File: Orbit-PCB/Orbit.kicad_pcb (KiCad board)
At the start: 2 copper layers, 303.2 x 145.3 mm, 296 parts, among them J1 PJ-3200B-4A, J10 Breakaway_Tabs, J11 PJ-3200B-4A, J12 AVR-ISP-6, J13 Breakaway_Tabs, J14 Breakaway_Tabs, J17 Breakaway_Tabs, J18 Breakaway_Tabs, J19 Breakaway_Tabs, J2 AVR-ISP-6, J20 Breakaway_Tabs, J3 Breakaway_Tabs, J5 Breakaway_Tabs, J6 Breakaway_Tabs, J7 Breakaway_Tabs, J9 Breakaway_Tabs, Q1 2N7002, Q2 2N7002, SW1 SW_Push, SW2 SW_Push, U1 ATmega32U4-MU, U2 PRTR5V0U2X, U3 ATmega32U4-MU, U4 PRTR5V0U2X, Y1 16MHz, Y2 16MHz

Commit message: Remove zones
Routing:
- net GND: track 1321.2 -> 0.00 mm, vias 32 -> 0
- net GNDA: track 1114.9 -> 0.00 mm, vias 39 -> 0
- net +5V: track 1023.8 -> 0.00 mm, vias 10 -> 0
- net +5VA: track 979.0 -> 0.00 mm, vias 8 -> 0
- net LEDGND: track 700.6 -> 0.00 mm, vias 12 -> 0
- net LEDGND-R: track 666.7 -> 0.00 mm, vias 16 -> 0
- net ROW0-R: track 242.9 -> 0.00 mm, vias 5 -> 0
- net ROW4-R: track 240.5 -> 0.00 mm, vias 8 -> 0
- net ROW0: track 195.1 -> 0.00 mm, vias 4 -> 0
- net ROW1-R: track 187.7 -> 0.00 mm, vias 2 -> 0
- net COL0: track 178.7 -> 0.00 mm
- net LEDIND-3-R: track 174.4 -> 0.00 mm, vias 4 -> 0
- net COL6: track 172.3 -> 0.00 mm, vias 2 -> 0
- net ROW1: track 171.7 -> 0.00 mm, vias 2 -> 0
- net COL1: track 171.4 -> 0.00 mm, vias 1 -> 0
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- removed copper zone on B.Cu, net GND
- removed copper zone on F.Cu, net GND
- removed copper zone on B.Cu, net GNDA
- removed copper zone on F.Cu, net GNDA

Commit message: Progress
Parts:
- removed R1, R45: 10k, Resistors_SMD:R_0805
- added FID4: Fiducial, Fiducials:Fiducial_1mm_Dia_2.54mm_Outer_CopperTop, B.Cu at (32.5, 15.9)
- added FID5: Fiducial, Fiducials:Fiducial_1mm_Dia_2.54mm_Outer_CopperTop, B.Cu at (331.0, 15.9)
- added FID6: Fiducial, Fiducials:Fiducial_1mm_Dia_2.54mm_Outer_CopperTop, B.Cu at (32.5, 156.4)
- moved J12 61.0 mm to (238.1, 92.1), turned to 180 degrees
- moved Q2 18.6 mm to (212.2, 128.3)
- moved R81 18.6 mm to (216.2, 128.3)
- moved R67 16.0 mm to (241.4, 105.3), turned to 180 degrees
- moved C11 14.5 mm to (239.4, 108.0), turned to 0 degrees
- moved D57 14.4 mm to (202.3, 100.1)
- moved R68 14.4 mm to (202.3, 105.6)
- moved D43 14.3 mm to (202.4, 61.9)
- moved D50 14.3 mm to (202.4, 81.0)
- moved D58 14.3 mm to (221.6, 97.6)
- moved R53 14.3 mm to (202.4, 67.5)
- moved R60 14.3 mm to (202.4, 86.5)
- moved R69 14.3 mm to (221.6, 103.2)
- moved R88 13.8 mm to (228.5, 106.3), turned to 0 degrees
- moved C10 12.5 mm to (237.1, 121.2), turned to 0 degrees
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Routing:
- net +5VA: track 0.00 -> 796.6 mm, vias 0 -> 10
- net LEDGND-R: track 0.00 -> 323.1 mm, vias 0 -> 6
- net GNDA: track 0.00 -> 300.5 mm, vias 0 -> 4
- net ROW0-R: track 0.00 -> 222.2 mm, vias 0 -> 4
- net ROW1-R: track 0.00 -> 192.5 mm, vias 0 -> 4
- net ROW2-R: track 0.00 -> 172.9 mm, vias 0 -> 4
- net COL5-R: track 0.00 -> 165.3 mm, vias 0 -> 1
- net ROW3-R: track 0.00 -> 156.5 mm, vias 0 -> 4
- net COL6-R: track 0.00 -> 154.9 mm
- net COL0-R: track 0.00 -> 147.7 mm, vias 0 -> 6
- net COL4-R: track 0.00 -> 133.8 mm, vias 0 -> 1
- net ROW4-R: track 0.00 -> 132.3 mm, vias 0 -> 2
- net COL3-R: track 0.00 -> 111.9 mm, vias 0 -> 1
- net LEDIND-1-R: track 0.00 -> 100.4 mm, vias 0 -> 2
- net LEDIND-3-R: track 0.00 -> 99.5 mm, vias 0 -> 2
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
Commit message: Continued progress
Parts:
- moved J2 23.6 mm to (154.4, 117.5), turned to 0 degrees
- moved D13 14.3 mm to (127.8, 59.5)
- moved D20 14.3 mm to (127.8, 78.6)
- moved D27 14.3 mm to (127.8, 97.6)
- moved R16 14.3 mm to (127.8, 65.1)
- moved R23 14.3 mm to (127.8, 84.1)
- moved D33 14.2 mm to (137.7, 118.3)
- moved C3 4.49 mm to (134.6, 112.8)
- moved R38 2.77 mm to (149.5, 125.2)
- moved C4 1.61 mm to (134.1, 118.5)
- moved R25 1.45 mm to (123.2, 103.3)
- moved R31 1.26 mm to (140.9, 102.8)
- moved C6 0.63 mm to (125.0, 105.7)
- moved R41 0.13 mm to (145.9, 43.0)
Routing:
- net LEDGND-R: track 323.1 -> 667.0 mm, vias 6 -> 21
- net GNDA: track 300.5 -> 544.8 mm, vias 4 -> 6
- net +5VA: track 796.6 -> 948.0 mm, vias 10 -> 14
- net GND: track 0.00 -> 136.8 mm
- net D+: track 0.00 -> 79.9 mm
- net D-: track 0.00 -> 79.0 mm
- net +5V: track 0.00 -> 73.5 mm
- net RESET-R: track 37.4 -> 84.6 mm, vias 2 -> 3
- net COL1-R: track 82.9 -> 117.4 mm, vias 2 -> 4
- net VCC: track 0.00 -> 24.7 mm, vias 0 -> 2
- net Net-(R44-Pad1): track 0.00 -> 18.6 mm, vias 0 -> 2
- net Net-(MX68-Pad4): track 0.00 -> 17.5 mm
- net Net-(D69-Pad2): track 0.00 -> 16.3 mm
- net COL4: track 0.00 -> 15.4 mm
- net COL3: track 0.00 -> 15.4 mm
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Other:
- net class POWER: trace_width 0.381 -> 0.254

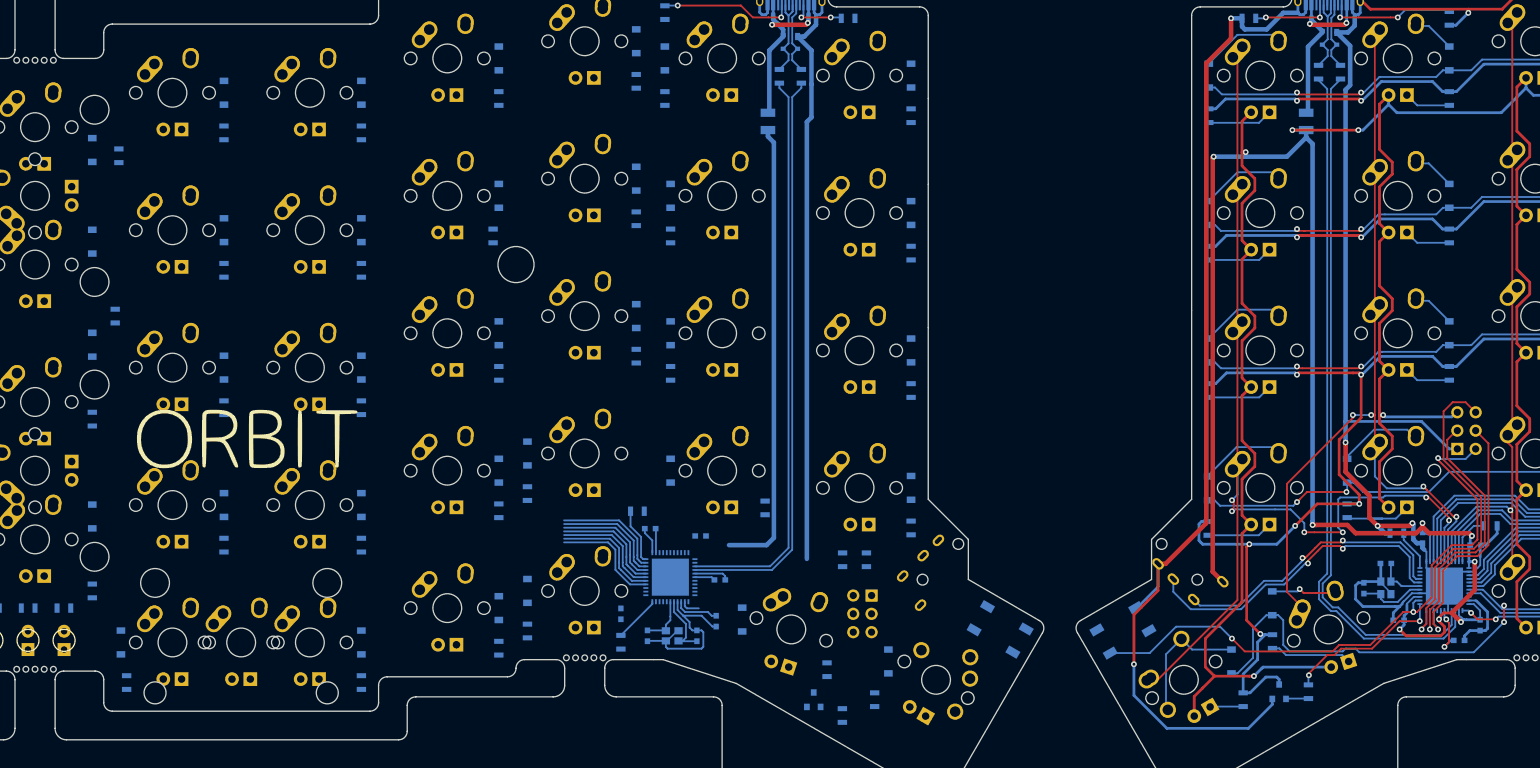
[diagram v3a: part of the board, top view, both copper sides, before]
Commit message: Add schottky divide to vcc/vbus
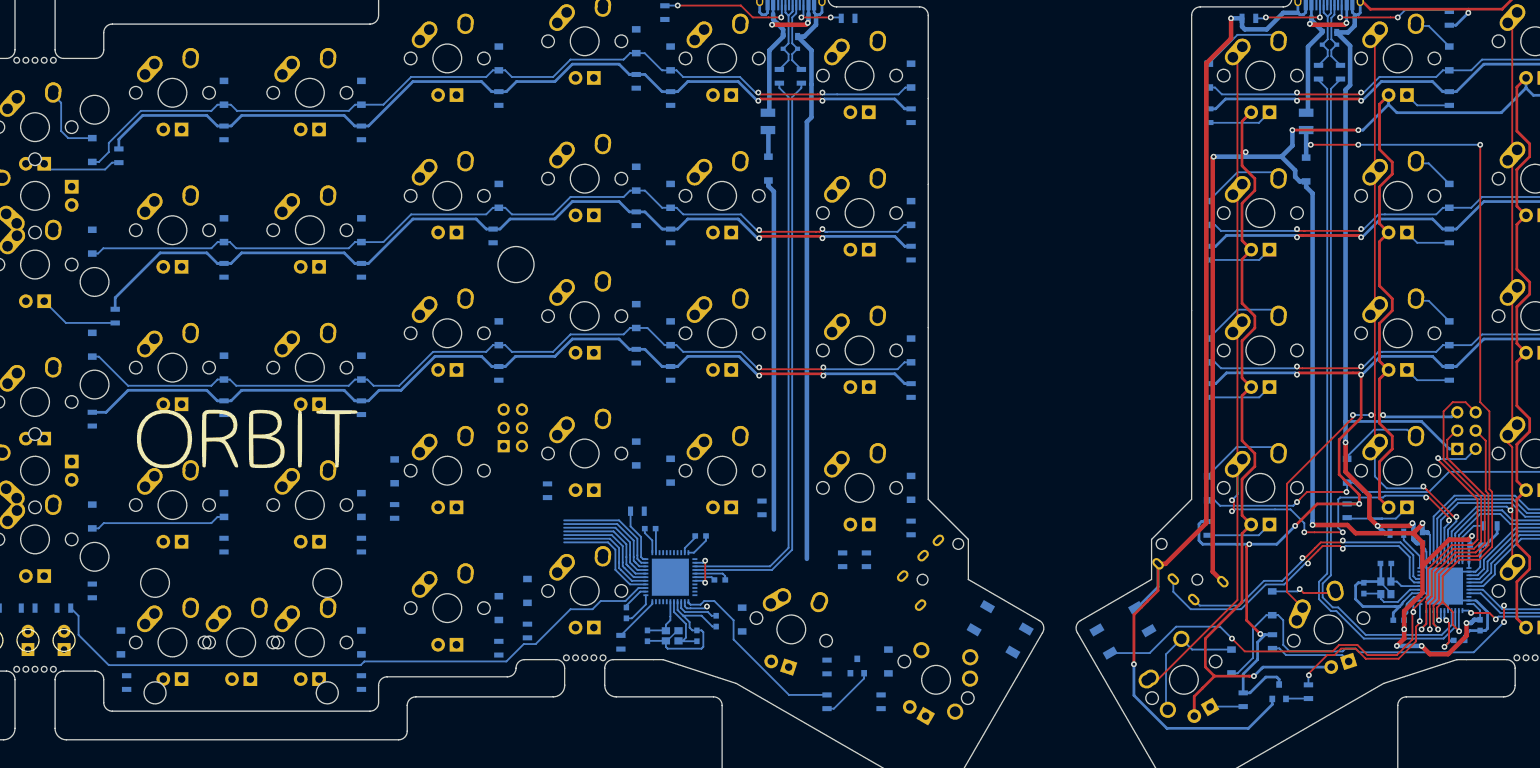
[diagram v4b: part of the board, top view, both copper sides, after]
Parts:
- added D75: Schottky, Diodes_SMD:D_SOD-123, B.Cu at (141.4, 55.8)
- added D76: Schottky, Diodes_SMD:D_SOD-123, B.Cu at (215.9, 55.9)
- moved J2 54.9 mm to (105.9, 91.7), turned to 180 degrees
- moved D26 15.1 mm to (123.0, 95.2)
- moved D25 14.4 mm to (89.5, 97.7)
- moved R29 14.4 mm to (89.5, 103.3)
- moved Q1 7.63 mm to (153.7, 124.7)
- moved R40 2.86 mm to (149.5, 129.7)
- moved R30 2.81 mm to (110.7, 100.4)
- moved R39 0.93 mm to (157.0, 129.7)
- moved D6 0.79 mm to (127.8, 40.5)
- moved R7 0.79 mm to (127.8, 46.0)
- moved C5 0.77 mm to (121.7, 117.3)
- moved R31 0.43 mm to (140.5, 102.8)
- moved R38 0.38 mm to (149.5, 124.8)
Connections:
- F1 pad 1: +5V -> VBUS
- F2 pad 1: +5VA -> VDC
- U1 pad 2: +5V -> VCC
- U1 pad 7: +5V -> VCC
- U3 pad 2: +5VA -> VDC
- U3 pad 7: +5VA -> VDC
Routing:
- net LEDGND: track 0.00 -> 373.8 mm, vias 0 -> 6
- net ROW0: track 0.00 -> 124.9 mm, vias 0 -> 2
- net ROW2: track 0.00 -> 123.7 mm, vias 0 -> 2
- net ROW1: track 0.00 -> 121.7 mm, vias 0 -> 2
- net VDC: track 0.00 -> 108.8 mm, vias 0 -> 5
- net LEDIND-1: track 0.00 -> 89.0 mm
- net LEDPWM: track 0.00 -> 26.6 mm
- net ROW3: track 0.00 -> 18.9 mm
- net Net-(MX8-Pad4): track 0.00 -> 11.1 mm
- net Net-(MX1-Pad4): track 0.00 -> 11.1 mm
- net Net-(D1-Pad2): track 0.00 -> 10.2 mm
- net GND: track 136.8 -> 144.4 mm
- net Net-(Q1-Pad1): track 0.00 -> 7.59 mm
- net +5V: track 73.5 -> 66.2 mm
- net VCC: track 24.7 -> 30.9 mm, vias 2 -> 4
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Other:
- net class POWER: trace_width 0.254 -> 0.381

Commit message: Finish routing
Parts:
- moved D33 14.1 mm to (151.8, 119.4)
- moved R31 10.7 mm to (129.8, 102.8)
- moved R10 4.84 mm to (153.8, 114.7), turned to 0 degrees
- moved R9 2.72 mm to (153.8, 111.6), turned to 0 degrees
- moved C6 0.97 mm to (124.6, 106.6)
- moved R25 0.54 mm to (122.8, 103.6)
- turned SW1 to 330 degrees
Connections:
- U1 pad 2: VCC -> VBUS
- U1 pad 7: VCC -> VBUS
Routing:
- net +5V: track 66.2 -> 1027.8 mm, vias 0 -> 15
- net GND: track 144.4 -> 567.2 mm, vias 0 -> 7
- net LEDGND: track 373.8 -> 670.1 mm, vias 6 -> 20
- net ROW4: track 0.00 -> 154.2 mm, vias 0 -> 7
- net COL1: track 15.4 -> 166.4 mm, vias 0 -> 1
- net COL0: track 15.4 -> 158.2 mm, vias 0 -> 2
- net COL6: track 15.4 -> 144.3 mm, vias 0 -> 4
- net RESET: track 3.94 -> 125.6 mm, vias 1 -> 4
- net COL2: track 15.4 -> 134.8 mm, vias 0 -> 1
- net ROW3: track 18.9 -> 133.5 mm, vias 0 -> 4
- net LEDIND-3: track 0.00 -> 109.6 mm, vias 0 -> 4
- net LEDIND-2: track 0.00 -> 102.8 mm, vias 0 -> 4
- net COL3: track 15.4 -> 115.2 mm, vias 0 -> 1
- net COL5: track 15.4 -> 112.3 mm, vias 0 -> 2
- net COL4: track 15.4 -> 95.2 mm, vias 0 -> 1
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
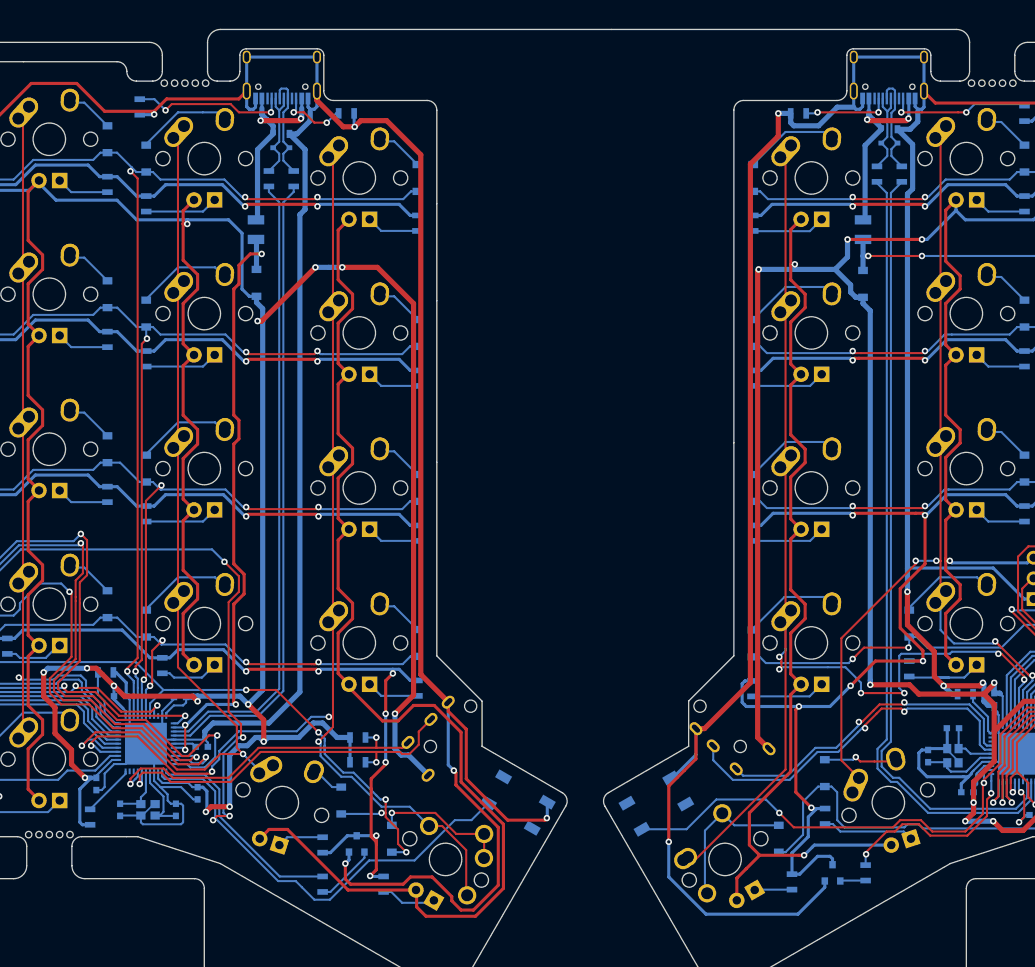
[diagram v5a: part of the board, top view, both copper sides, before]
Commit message: Finish reroute
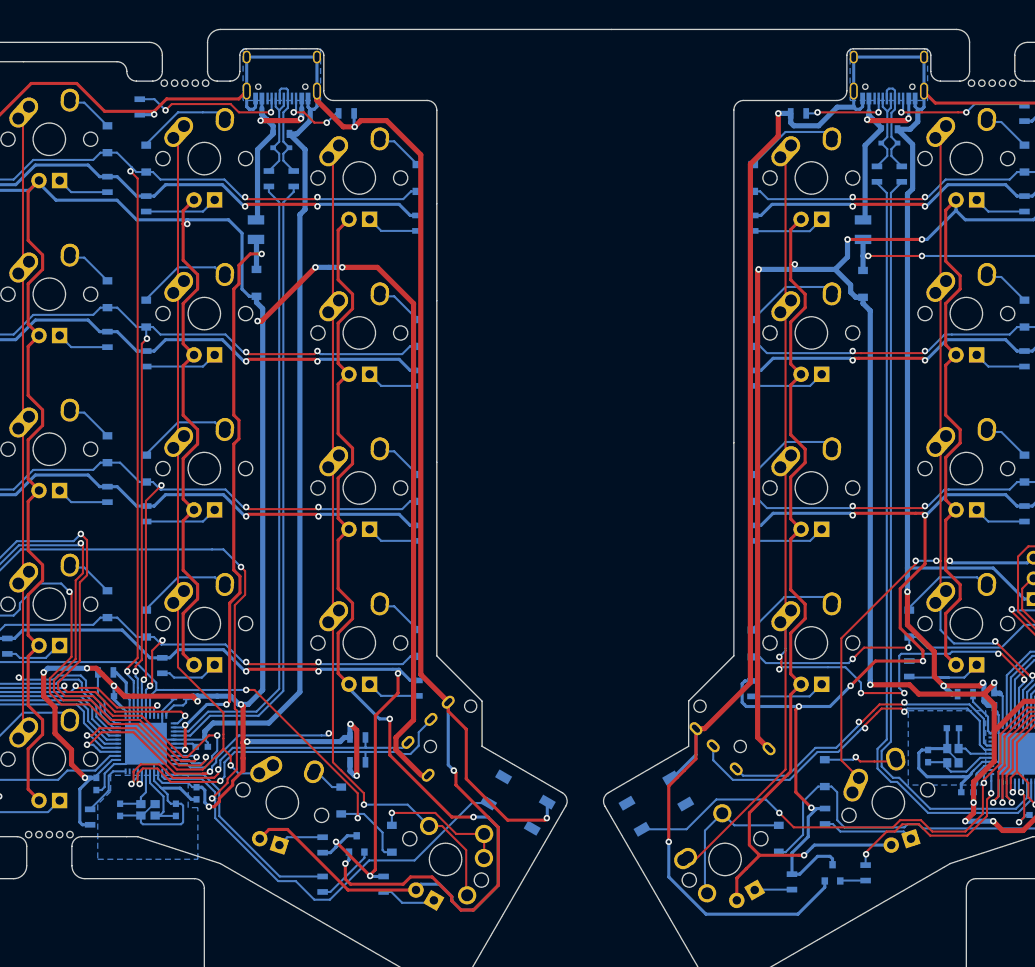
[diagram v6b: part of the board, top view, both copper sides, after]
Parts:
- moved C4 0.13 mm to (134.0, 118.5)
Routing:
- net ROW4: track 154.2 -> 146.9 mm, vias 7 -> 4
- net RESET: track 125.6 -> 121.1 mm, vias 4 -> 2
- net +5V: track 1027.8 -> 1024.3 mm, vias 15 -> 17
- net LEDGND: track 670.1 -> 673.0 mm, vias 20 -> 18
- net COL5: track 112.3 -> 110.1 mm
- net VBUS: track 77.0 -> 75.7 mm
- net HDETECT: track 6.47 -> 7.37 mm
- net COL6: track 144.3 -> 143.5 mm
- net SCL: track 46.0 -> 46.8 mm
- added copper zone on B.Cu, net GND
- added copper zone on B.Cu, net GNDA

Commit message: Final touch
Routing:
- net GND: track 566.9 -> 571.3 mm, vias 7 -> 6
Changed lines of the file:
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@@
   (via (at 42.418 98.806) (size 0.8) (drill 0.4) (layers F.Cu B.Cu) (net 1))
   (segment (start 44.958 101.346) (end 42.418 98.806) (width 0.381) (layer F.Cu) (net 1))
-  (segment (start 42.418 98.806) (end 42.418 97.536) (width 0.381) (layer B.Cu) (net 1))
-  (segment (start 42.418 97.536) (end 42.418 95.758) (width 0.381) (layer B.Cu) (net 1))
-  (segment (start 42.418 95.758) (end 44.323 93.853) (width 0.381) (layer B.Cu) (net 1))
-  (segment (start 44.323 93.853) (end 85.598 93.853) (width 0.381) (layer B.Cu) (net 1))
-  (segment (start 85.598 93.853) (end 88.646 90.805) (width 0.381) (layer B.Cu) (net 1))
-  (segment (start 88.646 90.805) (end 100.33 90.805) (width 0.381) (layer B.Cu) (net 1))
-  (via (at 102.235 94.234) (size 0.8) (drill 0.4) (layers F.Cu B.Cu) (net 1))
-  (segment (start 100.33 90.805) (end 102.235 92.71) (width 0.381) (layer B.Cu) (net 1))
-  (segment (start 102.235 92.71) (end 102.235 94.234) (width 0.381) (layer B.Cu) (net 1))
   (segment (start 123.759 103.632) (end 124.079 103.632) (width 0.381) (layer B.Cu) (net 1))
   (segment (start 125.337 104.89) (end 125.337 106.553) (width 0.381) (layer B.Cu) (net 1))
@@
   (segment (start 135.009 111.895) (end 135.009 111.633) (width 0.254) (layer B.Cu) (net 1))
   (segment (start 135.009 111.633) (end 135.009 110.879) (width 0.254) (layer B.Cu) (net 1))
-  (segment (start 104.648 94.234) (end 102.235 94.234) (width 0.381) (layer B.Cu) (net 1))
-  (segment (start 102.489 93.98) (end 102.235 94.234) (width 0.381) (layer F.Cu) (net 1))
-  (segment (start 102.489 88.138) (end 102.489 93.98) (width 0.381) (layer F.Cu) (net 1))
-  (segment (start 103.378 87.249) (end 102.489 88.138) (width 0.381) (layer F.Cu) (net 1))
-  (segment (start 102.489 70.739) (end 103.378 71.628) (width 0.381) (layer F.Cu) (net 1))
   (segment (start 128.778 34.671) (end 122.682 34.671) (width 0.381) (layer F.Cu) (net 1))
   (segment (start 119.253 31.242) (end 113.665 31.242) (width 0.381) (layer F.Cu) (net 1))
-  (segment (start 103.378 71.628) (end 103.378 87.249) (width 0.381) (layer F.Cu) (net 1))
-  (segment (start 113.665 31.242) (end 103.378 41.529) (width 0.381) (layer F.Cu) (net 1))
-  (segment (start 103.378 41.529) (end 103.378 66.548) (width 0.381) (layer F.Cu) (net 1))
-  (segment (start 102.489 67.437) (end 102.489 70.739) (width 0.381) (layer F.Cu) (net 1))
   (segment (start 122.682 34.671) (end 119.253 31.242) (width 0.381) (layer F.Cu) (net 1))
-  (segment (start 103.378 66.548) (end 102.489 67.437) (width 0.381) (layer F.Cu) (net 1))
   (via (at 152.273 127.127) (size 0.8) (drill 0.4) (layers F.Cu B.Cu) (net 1))
   (segment (start 152.72 125.714) (end 152.72 126.68) (width 0.381) (layer B.Cu) (net 1))
@@
   (segment (start 131.953 117.856) (end 129.921 117.856) (width 0.381) (layer B.Cu) (net 1))
   (segment (start 129.921 117.856) (end 129.667 117.856) (width 0.254) (layer B.Cu) (net 1))
+  (segment (start 113.665 31.242) (end 110.83925 31.242) (width 0.381) (layer F.Cu) (net 1))
+  (segment (start 110.83925 31.242) (end 109.140625 32.940625) (width 0.381) (layer F.Cu) (net 1))
+  (segment (start 109.140625 32.940625) (end 109.140625 67.230625) (width 0.381) (layer F.Cu) (net 1))
+  (segment (start 109.140625 67.230625) (end 109.601 67.691) (width 0.381) (layer F.Cu) (net 1))
+  (segment (start 109.601 67.691) (end 109.601 70.485) (width 0.381) (layer F.Cu) (net 1))
+  (segment (start 109.601 70.485) (end 109.140625 70.945375) (width 0.381) (layer F.Cu) (net 1))
+  (segment (start 109.140625 70.945375) (end 109.140625 94.853125) (width 0.381) (layer F.Cu) (net 1))
+  (segment (start 109.140625 94.853125) (end 107.95 96.04375) (width 0.381) (layer F.Cu) (net 1))
+  (segment (start 107.95 96.04375) (end 105.56875 96.04375) (width 0.381) (layer F.Cu) (net 1))
+  (segment (start 104.648 95.123) (end 104.648 94.234) (width 0.381) (layer F.Cu) (net 1))
+  (segment (start 105.56875 96.04375) (end 104.648 95.123) (width 0.381) (layer F.Cu) (net 1))
+  (segment (start 42.418 97.536) (end 42.418 98.806) (width 0.381) (layer B.Cu) (net 1))
+  (segment (start 42.418 95.758) (end 42.418 97.536) (width 0.381) (layer B.Cu) (net 1))
+  (segment (start 103.759 94.234) (end 100.33 90.805) (width 0.381) (layer B.Cu) (net 1))
+  (segment (start 104.648 94.234) (end 103.759 94.234) (width 0.381) (layer B.Cu) (net 1))
+  (segment (start 100.33 90.805) (end 88.646 90.805) (width 0.381) (layer B.Cu) (net 1))
+  (segment (start 88.646 90.805) (end 85.598 93.853) (width 0.381) (layer B.Cu) (net 1))
+  (segment (start 85.598 93.853) (end 44.323 93.853) (width 0.381) (layer B.Cu) (net 1))
+  (segment (start 44.323 93.853) (end 42.418 95.758) (width 0.381) (layer B.Cu) (net 1))
   (segment (start 127.141 119.823) (end 127.141 118.985) (width 0.254) (layer B.Cu) (net 2))
   (segment (start 127.762 118.364) (end 127.762 117.856) (width 0.254) (layer B.Cu) (net 2))

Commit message: Please commit properly this time
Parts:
- moved J2 19.5 mm to (125.4, 92.1)
- moved D27 14.3 mm to (142.1, 97.6)
- moved D26 14.3 mm to (108.7, 95.2)
- moved R30 2.02 mm to (108.7, 100.8)
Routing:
- net RESET: track 121.1 -> 101.4 mm
- net MISO: track 68.0 -> 54.3 mm
- net MOSI: track 61.3 -> 47.8 mm, vias 2 -> 1
- net SCK: track 58.3 -> 46.2 mm, vias 2 -> 1
- net ROW3: track 133.5 -> 142.1 mm, vias 4 -> 5
- net Net-(D26-Pad2): track 5.82 -> 13.6 mm
- net Net-(D27-Pad2): track 11.9 -> 5.82 mm
- net GND: track 571.3 -> 567.0 mm, vias 6 -> 7
- net +5V: track 1024.3 -> 1022.4 mm, vias 17 -> 18
- net Net-(MX26-Pad4): track 7.27 -> 9.09 mm
- net LEDGND: track 673.0 -> 671.8 mm, vias 18 -> 17
- net ROW1: track 170.2 -> 171.4 mm
- net ROW0: track 193.7 -> 194.8 mm
- net ROW2: track 153.5 -> 154.7 mm
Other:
- net class POWER: trace_width 0.381 -> 0.635
